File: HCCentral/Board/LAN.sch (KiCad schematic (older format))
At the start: 28 parts, among them IC1 ENC28J60-I/SO, J1 RJ45-TRJ0011BANL, P2 ANT_433, P3 ANT_866, U2 RFM69CW, U3 RFM69CW, Y1 25Mhz

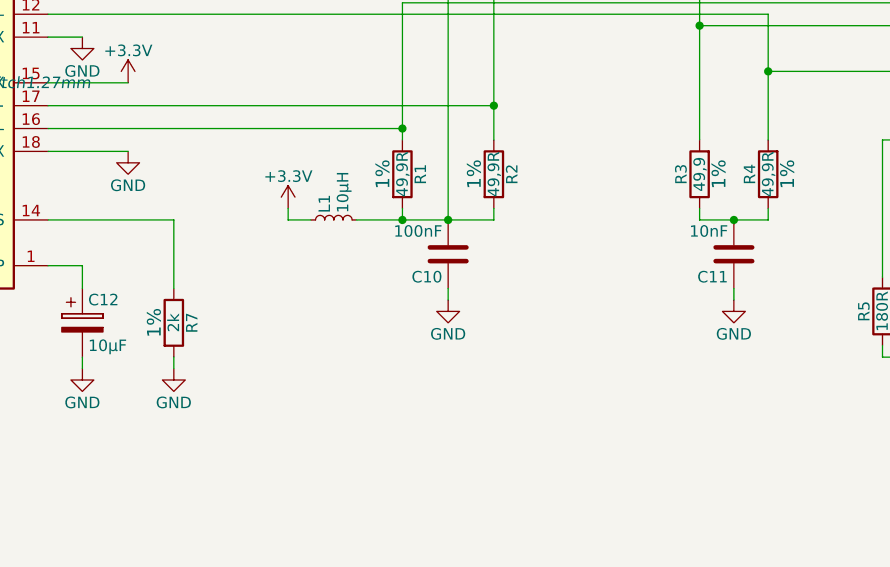
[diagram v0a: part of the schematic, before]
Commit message: Deleted Gerbers, Updated V1.5
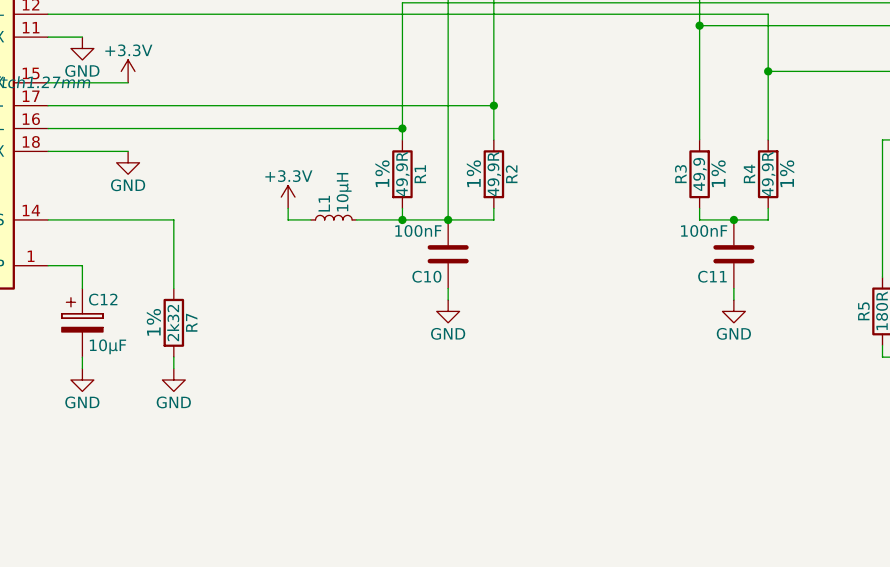
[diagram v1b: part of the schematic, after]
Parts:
- C11: value 10nF -> 100nF
- R7: value 2k -> 2k32
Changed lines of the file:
@@
 P 4550 3500
 F 0 "R7" V 4630 3500 50  0000 C CNN
-F 1 "2k" V 4550 3500 50  0000 C CNN
+F 1 "2k32" V 4550 3500 50  0000 C CNN
 F 2 "Resistors_SMD:R_0805" V 4480 3500 30  0001 C CNN
 F 3 "" H 4550 3500 30  0000 C CNN
@@
 P 7000 3200
 F 0 "C11" H 7025 3300 50  0000 L CNN
-F 1 "10nF" H 7025 3100 50  0000 L CNN
+F 1 "100nF" H 7025 3100 50  0000 L CNN
 F 2 "Capacitors_SMD:C_0805" H 7038 3050 30  0001 C CNN
 F 3 "" H 7000 3200 60  0000 C CNN
